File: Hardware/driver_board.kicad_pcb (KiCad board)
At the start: 2 copper layers, 48 parts, among them P1 CONN_4X2, P10 CONN_4X2, P11 CONN_4X2, P12 CONN_4X2, P13 CONN_4X2, P14 CONN_4X2, P15 CONN_4X2, P16 CONN_4X2, P17 CONN_4X2, P18 CONN_4X2, P19 CONN_4X2, P2 CONN_4X2, P20 CONN_4X2, P21 CONN_4X2, P22 CONN_4X2, P23 CONN_4X2, P24 CONN_4X2, P3 CONN_4X2, P4 CONN_4X2, P5 CONN_4X2, P6 CONN_4X2, P7 CONN_4X2, P8 CONN_4X2, P9 CONN_4X2, U1 TLC590, U10 TLC590, U11 TLC590, U12 TLC590, U2 TLC590, U3 TLC590, U4 TLC590, U5 TLC590, U6 TLC590, U7 TLC590, U8 TLC590, U9 TLC590

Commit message: progress on board
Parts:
- added C1: C, Capacitors_SMD:c_0805, F.Cu at (122.5, 56.5)
- added C10: C, Capacitors_SMD:c_0805, F.Cu at (208.0, 77.0)
- added C11: C, Capacitors_SMD:c_0805, F.Cu at (208.0, 97.0)
- added C12: C, Capacitors_SMD:c_0805, F.Cu at (208.0, 116.2)
- added C2: C, Capacitors_SMD:c_0805, F.Cu at (122.5, 77.5)
- added C3: C, Capacitors_SMD:c_0805, F.Cu at (122.5, 97.0)
- added C4: C, Capacitors_SMD:c_0805, F.Cu at (122.5, 117.0)
- added C5: C, Capacitors_SMD:c_0805, F.Cu at (165.2, 57.0)
- added C6: C, Capacitors_SMD:c_0805, F.Cu at (165.2, 77.0)
- added C7: C, Capacitors_SMD:c_0805, F.Cu at (165.2, 97.0)
- added C8: C, Capacitors_SMD:c_0805, F.Cu at (165.2, 116.2)
- added C9: C, Capacitors_SMD:c_0805, F.Cu at (208.0, 57.0)
- added P25: CONN_4X2, Pin_Headers:Pin_Header_Straight_2x04, F.Cu at (131.0, 37.5)
- added P26: CONN_4X2, Pin_Headers:Pin_Header_Straight_2x04, F.Cu at (153.5, 50.5)
- added P27: CONN_4X2, Pin_Headers:Pin_Header_Straight_2x04, F.Cu at (170.2, 50.5)
- added R13: R, Resistors_SMD:Resistor_SMD0805_HandSoldering, F.Cu at (121.0, 32.5)
- moved R12 91.6 mm to (211.0, 115.2)
- moved U12 90.9 mm to (208.8, 125.5)
- moved R11 90.6 mm to (211.0, 96.0)
- moved U11 89.5 mm to (208.8, 105.5)
- moved R10 89.3 mm to (211.0, 76.0)
- moved R8 89.1 mm to (168.2, 115.2)
- moved R4 88.4 mm to (127.0, 116.0)
- moved U8 88.3 mm to (165.8, 125.5)
- moved R9 88.1 mm to (211.0, 56.0)
- moved P20 88.1 mm to (191.8, 120.0)
- moved U10 88.1 mm to (208.8, 85.5)
- moved R7 88.1 mm to (168.2, 96.0)
- moved U4 87.2 mm to (124.5, 125.5)
- moved R3 87.0 mm to (127.0, 96.0)
- moved P19 86.8 mm to (191.8, 100.0)
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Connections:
- P1 pad 1: /ROA1 -> /ROA2
- P1 pad 2: /ROA2 -> /ROA1
- P1 pad 3: /ROA3 -> /ROA4
- P1 pad 4: /ROA4 -> /ROA3
- P1 pad 5: /ROA5 -> /ROA6
- P1 pad 6: /ROA6 -> /ROA5
- P1 pad 7: /ROA7 -> /ROA8
- P1 pad 8: /ROA8 -> /ROA7
- P10 pad 1: /GOB1 -> /GOB2
- P10 pad 2: /GOB2 -> /GOB1
- P10 pad 3: /GOB3 -> /GOB4
- P10 pad 4: /GOB4 -> /GOB3
- P10 pad 5: /GOB5 -> /GOB6
- P10 pad 6: /GOB6 -> /GOB5
- P10 pad 7: /GOB7 -> /GOB8
- P10 pad 8: /GOB8 -> /GOB7
- P11 pad 1: /GOC1 -> /GOC2
- P11 pad 2: /GOC2 -> /GOC1
- P11 pad 3: /GOC3 -> /GOC4
- P11 pad 4: /GOC4 -> /GOC3
- P11 pad 5: /GOC5 -> /GOC6
- P11 pad 6: /GOC6 -> /GOC5
- P11 pad 7: /GOC7 -> /GOC8
- P11 pad 8: /GOC8 -> /GOC7
- P12 pad 1: /GOD1 -> /GOD2
- P12 pad 2: /GOD2 -> /GOD1
- P12 pad 3: /GOD3 -> /GOD4
- P12 pad 4: /GOD4 -> /GOD3
- P12 pad 5: /GOD5 -> /GOD6
- P12 pad 6: /GOD6 -> /GOD5
- P12 pad 7: /GOD7 -> /GOD8
- P12 pad 8: /GOD8 -> /GOD7
- P17 pad 1: /BOA1 -> /BOA2
- P17 pad 2: /BOA2 -> /BOA1
- P17 pad 3: /BOA3 -> /BOA4
- P17 pad 4: /BOA4 -> /BOA3
- P17 pad 5: /BOA5 -> /BOA6
- P17 pad 6: /BOA6 -> /BOA5
- P17 pad 7: /BOA7 -> /BOA8
- P17 pad 8: /BOA8 -> /BOA7
- P18 pad 1: /BOB1 -> /BOB2
- P18 pad 2: /BOB2 -> /BOB1
- P18 pad 3: /BOB3 -> /BOB4
- P18 pad 4: /BOB4 -> /BOB3
- P18 pad 5: /BOB5 -> /BOB6
- P18 pad 6: /BOB6 -> /BOB5
- P18 pad 7: /BOB7 -> /BOB8
- P18 pad 8: /BOB8 -> /BOB7
- P19 pad 1: /BOC1 -> /BOC2
- P19 pad 2: /BOC2 -> /BOC1
- P19 pad 3: /BOC3 -> /BOC4
- P19 pad 4: /BOC4 -> /BOC3
- P19 pad 5: /BOC5 -> /BOC6
- P19 pad 6: /BOC6 -> /BOC5
- P19 pad 7: /BOC7 -> /BOC8
- P19 pad 8: /BOC8 -> /BOC7
- P2 pad 1: /ROB1 -> /ROB2
- P2 pad 2: /ROB2 -> /ROB1
- P2 pad 3: /ROB3 -> /ROB4
- P2 pad 4: /ROB4 -> /ROB3
- P2 pad 5: /ROB5 -> /ROB6
- P2 pad 6: /ROB6 -> /ROB5
- P2 pad 7: /ROB7 -> /ROB8
- P2 pad 8: /ROB8 -> /ROB7
- P20 pad 1: /BOD1 -> /BOD2
- P20 pad 2: /BOD2 -> /BOD1
- P20 pad 3: /BOD3 -> /BOD4
- P20 pad 4: /BOD4 -> /BOD3
- P20 pad 5: /BOD5 -> /BOD6
- P20 pad 6: /BOD6 -> /BOD5
- P20 pad 7: /BOD7 -> /BOD8
- P20 pad 8: /BOD8 -> /BOD7
- P3 pad 1: /ROC1 -> /ROC2
- P3 pad 2: /ROC2 -> /ROC1
- P3 pad 3: /ROC3 -> /ROC4
- P3 pad 4: /ROC4 -> /ROC3
- P3 pad 5: /ROC5 -> /ROC6
- P3 pad 6: /ROC6 -> /ROC5
- P3 pad 7: /ROC7 -> /ROC8
- P3 pad 8: /ROC8 -> /ROC7
- P4 pad 1: /ROD1 -> /ROD2
- P4 pad 2: /ROD2 -> /ROD1
- P4 pad 3: /ROD3 -> /ROD4
- P4 pad 4: /ROD4 -> /ROD3
- P4 pad 5: /ROD5 -> /ROD6
- P4 pad 6: /ROD6 -> /ROD5
- P4 pad 7: /ROD7 -> /ROD8
- P4 pad 8: /ROD8 -> /ROD7
- P9 pad 1: /GOA1 -> /GOA2
- P9 pad 2: /GOA2 -> /GOA1
- P9 pad 3: /GOA3 -> /GOA4
- P9 pad 4: /GOA4 -> /GOA3
- P9 pad 5: /GOA5 -> /GOA6
- P9 pad 6: /GOA6 -> /GOA5
- P9 pad 7: /GOA7 -> /GOA8
- P9 pad 8: /GOA8 -> /GOA7
- R10 pad 1: Net-(R10-Pad1) -> GND
- R12 pad 1: Net-(R12-Pad1) -> GND
- R2 pad 1: Net-(R2-Pad1) -> GND
- R4 pad 1: Net-(R4-Pad1) -> GND
- R6 pad 1: Net-(R6-Pad1) -> GND
- R8 pad 1: Net-(R8-Pad1) -> GND
- U1 pad 26: /dcprg -> +3.3V
- U1 pad 28: /vcc -> +3.3V
- U10 pad 26: /dcprg -> +3.3V
- U10 pad 28: /vcc -> +3.3V
- U11 pad 26: /dcprg -> +3.3V
- U11 pad 28: /vcc -> +3.3V
- U12 pad 24: Net-(U12-Pad24) -> (no net)
- U12 pad 26: /dcprg -> +3.3V
- U12 pad 28: /vcc -> +3.3V
- U2 pad 26: /dcprg -> +3.3V
- U2 pad 28: /vcc -> +3.3V
- U3 pad 26: /dcprg -> +3.3V
- U3 pad 28: /vcc -> +3.3V
- U4 pad 26: /dcprg -> +3.3V
- U4 pad 28: /vcc -> +3.3V
- U5 pad 26: /dcprg -> +3.3V
- U5 pad 28: /vcc -> +3.3V
- U6 pad 26: /dcprg -> +3.3V
- U6 pad 28: /vcc -> +3.3V
- U7 pad 26: /dcprg -> +3.3V
- U7 pad 28: /vcc -> +3.3V
- U8 pad 26: /dcprg -> +3.3V
- U8 pad 28: /vcc -> +3.3V
- U9 pad 26: /dcprg -> +3.3V
- U9 pad 28: /vcc -> +3.3V
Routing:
- added copper zone on B.Cu, net GND
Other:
- net class Default: clearance 0.254 -> 0.0254
- rule trace_clearance: 0.254 -> 0.0254
- rule trace_min: 0.254 -> 6.4516
- rule via_min_size: 0.889 -> 22.5806

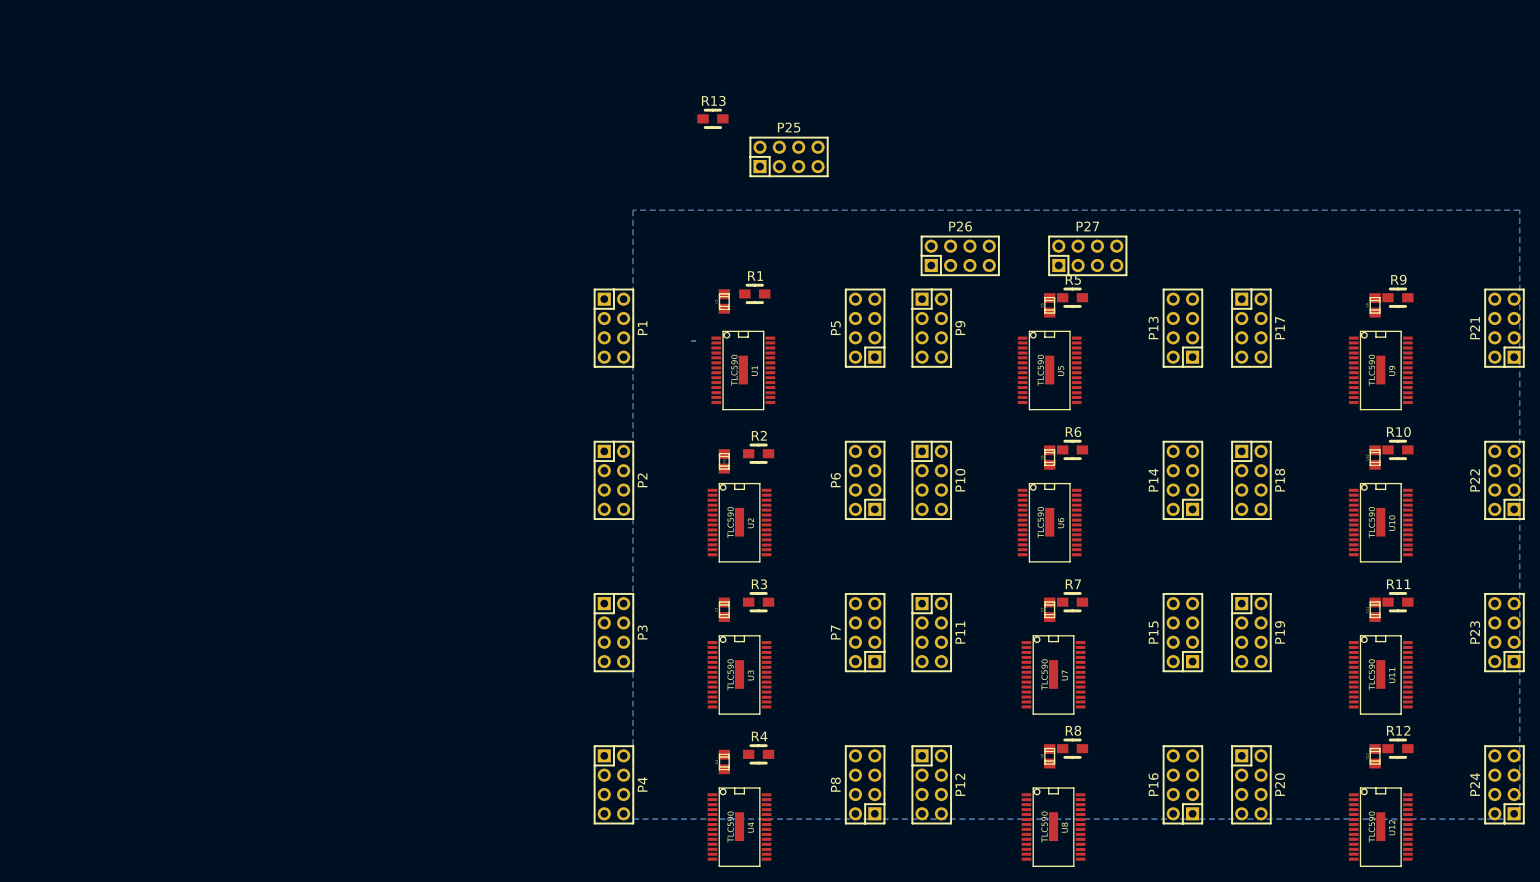
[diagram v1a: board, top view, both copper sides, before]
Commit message: moving from kicad to eagle. The boards came ba ck with crazy shorts in them so i am re-designing them in kicad.
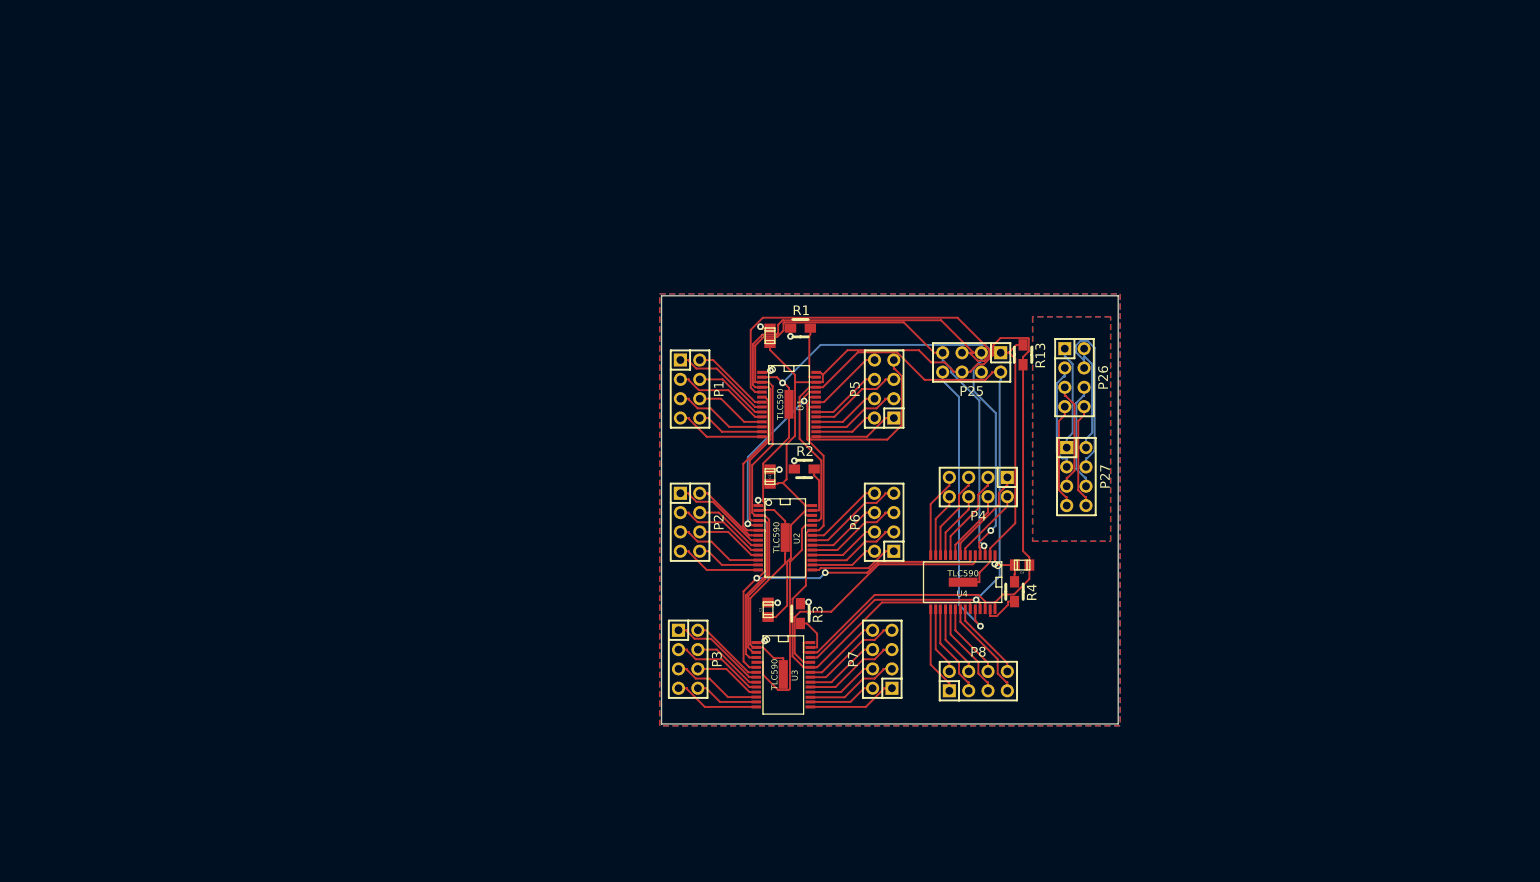
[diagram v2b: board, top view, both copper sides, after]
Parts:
- removed C10, C11, C12, C5, C6, C7, C8, C9: C, Capacitors_SMD:c_0805
- removed P10, P11, P12, P13, P14, P15, P16, P17, P18, P19, P20, P21, P22, P23, P24, P9: CONN_4X2, Pin_Headers:Pin_Header_Straight_2x04
- removed R10, R11, R12, R5, R6, R7, R8, R9: R, Resistors_SMD:Resistor_SMD0805_HandSoldering
- removed U10, U11, U12, U5, U6, U7, U8, U9: TLC590, TLC5940:SSOP-28H
- moved P4 61.8 mm to (155.9, 80.9), turned to 180 degrees
- moved R13 51.2 mm to (161.8, 63.5), turned to 270 degrees
- moved C4 46.9 mm to (161.6, 91.1), turned to 180 degrees
- moved U4 43.5 mm to (153.9, 93.4), turned to 180 degrees
- moved R4 39.8 mm to (160.6, 94.6), turned to 270 degrees
- moved P25 36.1 mm to (155.0, 64.5), turned to 180 degrees
- moved P27 29.0 mm to (168.8, 79.5), turned to 270 degrees
- moved P26 21.9 mm to (168.5, 66.5), turned to 270 degrees
- moved P8 20.2 mm to (155.9, 106.4), turned to 0 degrees
- moved P1 12.8 mm to (118.0, 68.0)
- moved P2 11.4 mm to (118.0, 85.5)
- moved P3 10.4 mm to (117.8, 103.5)
- moved P5 8.38 mm to (143.5, 68.0)
- moved C1 7.50 mm to (128.5, 61.0)
- moved R1 7.50 mm to (132.5, 60.0)
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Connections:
- P25 pad 8: (no net) -> /sin_E
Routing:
- net +3.3V: track 0.00 -> 155.2 mm
- net /blank: track 0.00 -> 120.4 mm, vias 0 -> 1
- net /sclk: track 0.00 -> 111.5 mm, vias 0 -> 1
- net /gsclk: track 0.00 -> 107.0 mm, vias 0 -> 1
- net /xlat: track 0.00 -> 104.1 mm, vias 0 -> 1
- net /vprg: track 0.00 -> 72.3 mm, vias 0 -> 2
- net /xerr: track 0.00 -> 66.8 mm
- net /sin: track 0.00 -> 48.2 mm
- net /sin_E: track 0.00 -> 37.9 mm, vias 0 -> 1
- net /sin_D: track 0.00 -> 34.9 mm
- net /sin_C: track 0.00 -> 30.2 mm
- net /ROA15: track 0.00 -> 27.0 mm
- net /sin_B: track 0.00 -> 23.0 mm, vias 0 -> 2
- net /L4: track 0.00 -> 22.7 mm
- net GND: track 0.00 -> 16.4 mm, vias 0 -> 10
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- added copper zone on F.Cu, net GND
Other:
- board outline added: 60 x 56.2 mm
